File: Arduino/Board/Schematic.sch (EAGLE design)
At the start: 59 parts, among them Q1 NTF3055L108, Q2 NTF3055L108, Q3 NTF3055L108, Q4 MOSFET-NCHANNELAO3404A

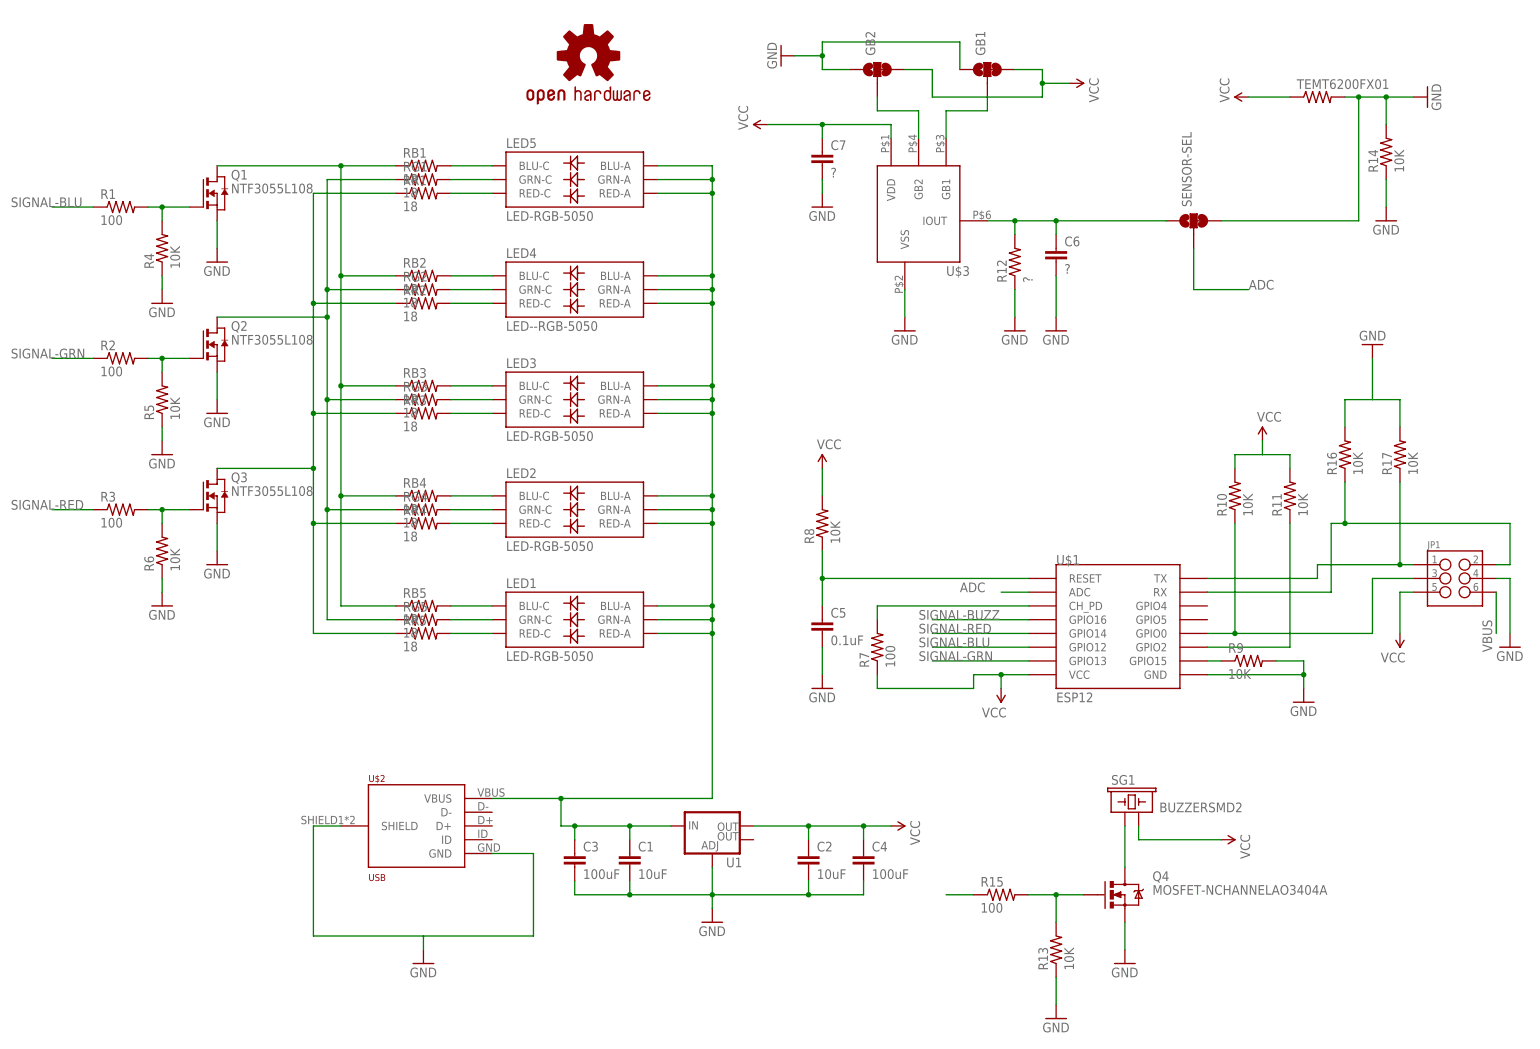
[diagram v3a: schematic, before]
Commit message: small fixes to the board.
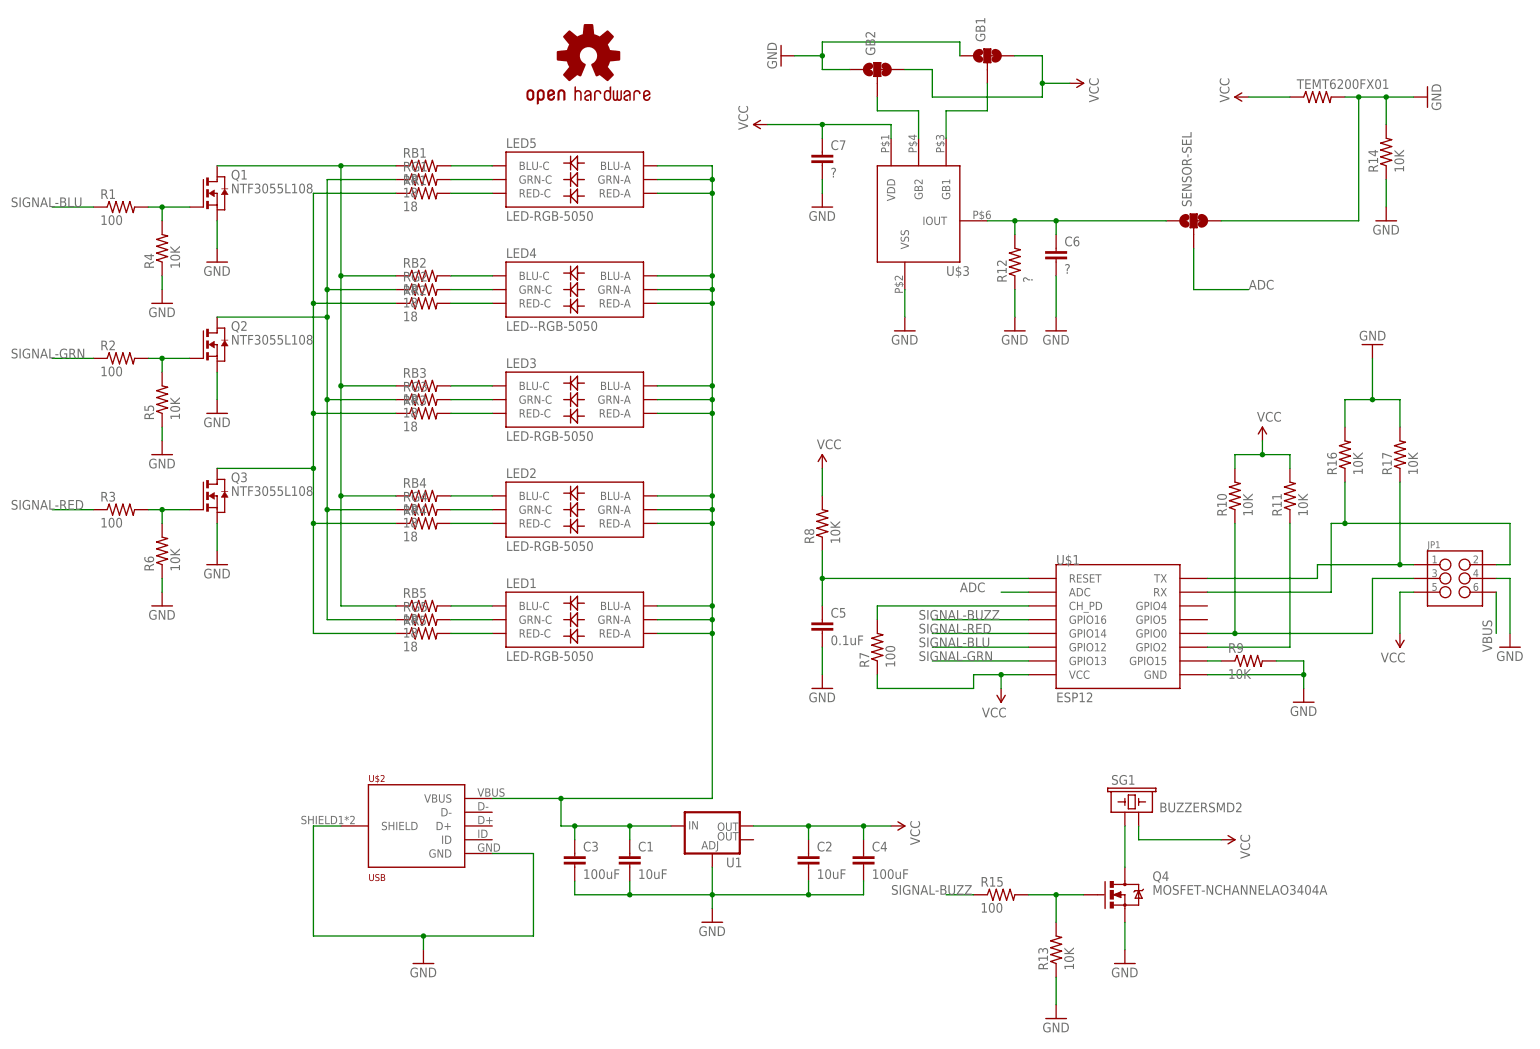
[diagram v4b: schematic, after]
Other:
- moved on the sheet: GB1
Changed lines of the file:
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@@
 <instance part="GND14" gate="1" x="96.52" y="139.7"/>
 <instance part="LOGO1" gate="G$1" x="38.1" y="190.5"/>
-<instance part="GB1" gate="G$1" x="111.76" y="187.96" rot="R90"/>
+<instance part="GB1" gate="G$1" x="111.76" y="190.5" rot="R90"/>
 <instance part="GB2" gate="G$1" x="91.44" y="187.96" rot="R90"/>
 <instance part="GND15" gate="1" x="73.66" y="190.5" rot="R270"/>
@@
 <wire x1="7.62" y1="27.94" x2="7.62" y2="25.4" width="0.1524" layer="91"/>
 <pinref part="GND2" gate="1" pin="GND"/>
+<junction x="7.62" y="27.94"/>
 </segment>
 <segment>
@@
 <segment>
 <pinref part="GB1" gate="G$1" pin="1"/>
-<wire x1="106.68" y1="187.96" x2="106.68" y2="193.04" width="0.1524" layer="91"/>
+<wire x1="106.68" y1="190.5" x2="106.68" y2="193.04" width="0.1524" layer="91"/>
 <wire x1="106.68" y1="193.04" x2="81.28" y2="193.04" width="0.1524" layer="91"/>
 <wire x1="81.28" y1="193.04" x2="81.28" y2="190.5" width="0.1524" layer="91"/>
@@
 <pinref part="GND21" gate="1" pin="GND"/>
 <wire x1="182.88" y1="127" x2="182.88" y2="134.62" width="0.1524" layer="91"/>
+<junction x="182.88" y="127"/>
 </segment>
 </net>
@@
 <wire x1="162.56" y1="116.84" x2="162.56" y2="119.38" width="0.1524" layer="91"/>
 <pinref part="SUPPLY5" gate="G$1" pin="VCC"/>
+<junction x="162.56" y="116.84"/>
 </segment>
 <segment>
@@
 <wire x1="121.92" y1="182.88" x2="121.92" y2="185.42" width="0.1524" layer="91"/>
 <pinref part="GB1" gate="G$1" pin="3"/>
-<wire x1="121.92" y1="185.42" x2="121.92" y2="187.96" width="0.1524" layer="91"/>
-<wire x1="121.92" y1="187.96" x2="116.84" y2="187.96" width="0.1524" layer="91"/>
+<wire x1="121.92" y1="185.42" x2="121.92" y2="190.5" width="0.1524" layer="91"/>
+<wire x1="121.92" y1="190.5" x2="116.84" y2="190.5" width="0.1524" layer="91"/>
 <wire x1="121.92" y1="185.42" x2="127" y2="185.42" width="0.1524" layer="91"/>
 <pinref part="SUPPLY6" gate="G$1" pin="VCC"/>
@@
 <wire x1="104.14" y1="180.34" x2="111.76" y2="180.34" width="0.1524" layer="91"/>
 <pinref part="GB1" gate="G$1" pin="2"/>
-<wire x1="111.76" y1="180.34" x2="111.76" y2="182.88" width="0.1524" layer="91"/>
+<wire x1="111.76" y1="180.34" x2="111.76" y2="185.42" width="0.1524" layer="91"/>
 </segment>
 </net>
@@
 <pinref part="R15" gate="G$1" pin="1"/>
 <wire x1="109.22" y1="35.56" x2="104.14" y2="35.56" width="0.1524" layer="91"/>
+<label x="93.98" y="35.56" size="1.778" layer="95"/>
 </segment>
 </net>
@@
 </sheet>
 </sheets>
+<errors>
+</errors>
 </schematic>
 </drawing>

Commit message: updated board (Rev. 3)
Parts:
- removed C6, C7: ?, SparkFun-Capacitors:CAP0603-CAP
- removed GB1, GB2, SENSOR-SEL: JUMPER-PAD-3-2OF3_NC_BY_TRACE_LARGE, SparkFun-Passives:JUMPER-PAD-3-2OF3_NC_BY_TRACE_LARGE
- removed R12: ?, SparkFun-Passives:RESISTOR0805-RES
- removed U$3: NOA1212, MCustom:NOA1212
- Q1, Q2, Q3: device zetex:NMOSSOT223 -> MCustom:NMOSSOT223'HEATSINK'
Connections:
- removed net N$1111: C6.1, R12.2, SENSOR-SEL.1, U$3.IOUT
- removed net N$51: GB2.2, U$3.GB2
- removed net N$54: GB1.2, U$3.GB1
- net ADC: now also R14.2, TEMT6200FX01.2; no longer SENSOR-SEL.2
- net GND: no longer C6.2, C7.2, GB1.1, GB2.1, R12.1, R14.2, SENSOR-SEL.3, TEMT6200FX01.2, U$3.VSS
- net VCC: no longer C7.1, GB1.3, GB2.3, U$3.VDD
